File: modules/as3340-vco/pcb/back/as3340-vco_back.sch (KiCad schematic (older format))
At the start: 34 parts, among them J1 Conn_02x08_Odd_Even, J2 Conn_01x09, U1 AS3340, U2 L79L05_TO92

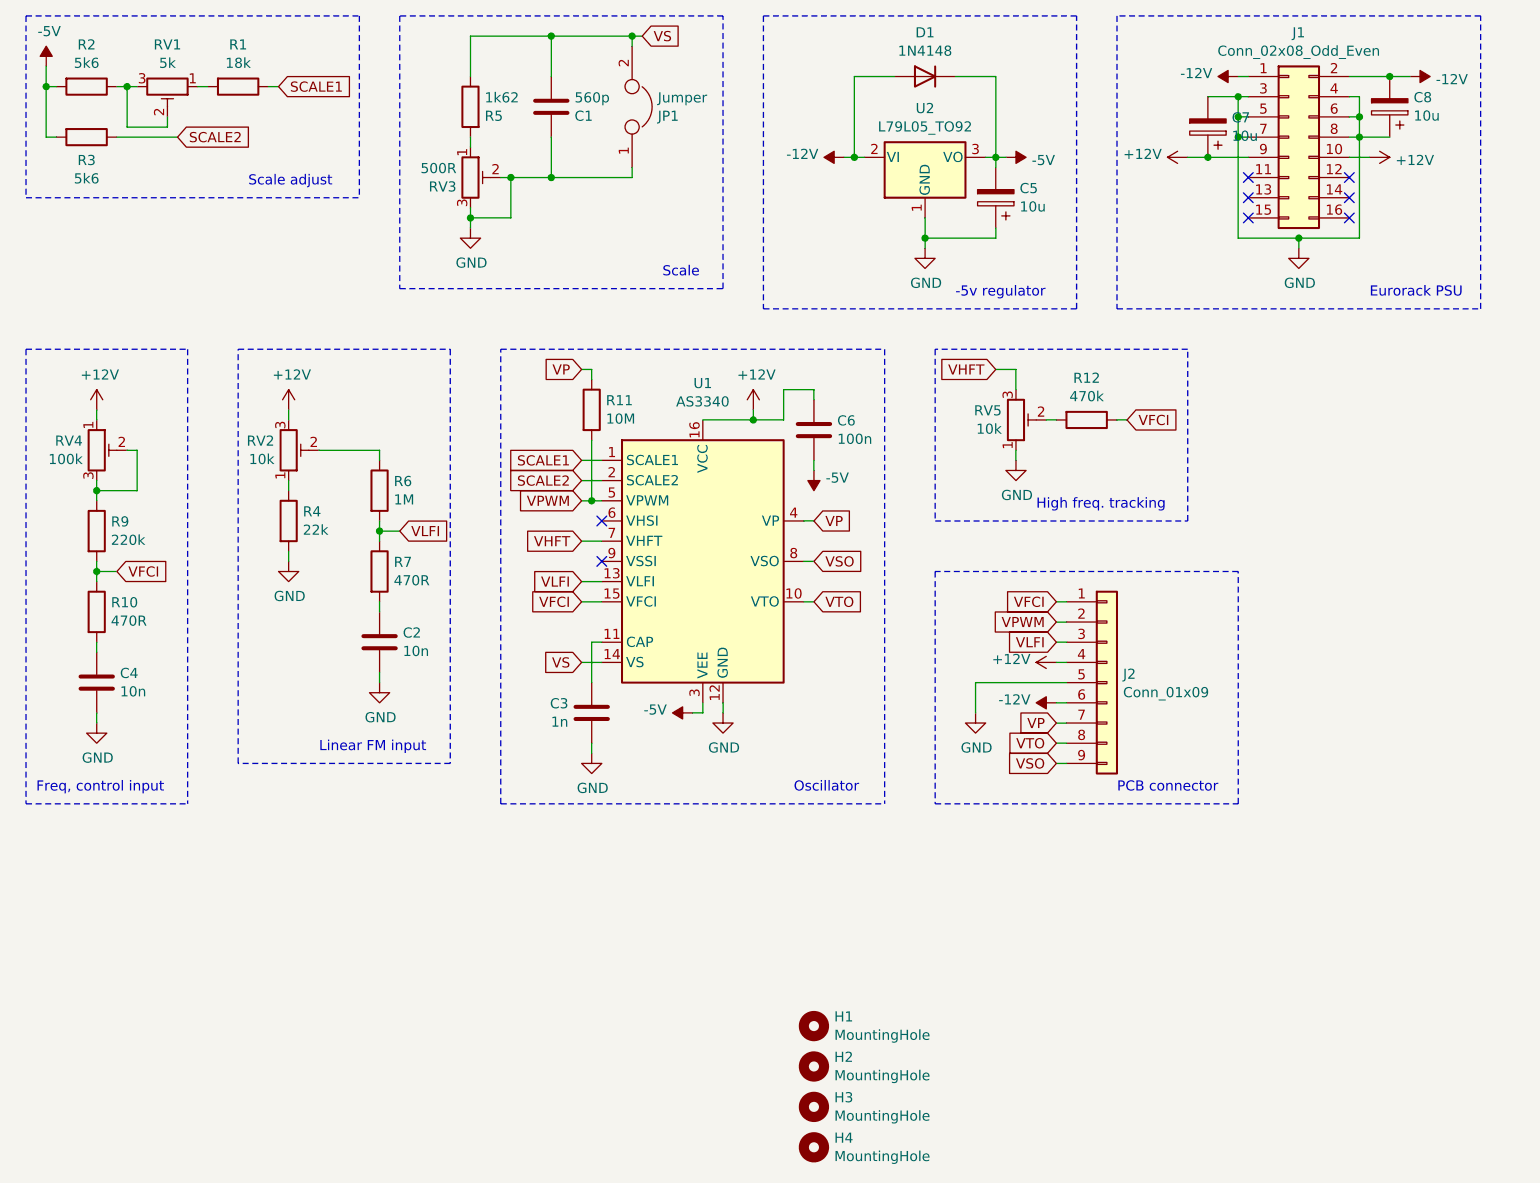
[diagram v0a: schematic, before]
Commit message: modules: as3340-vco: fix references
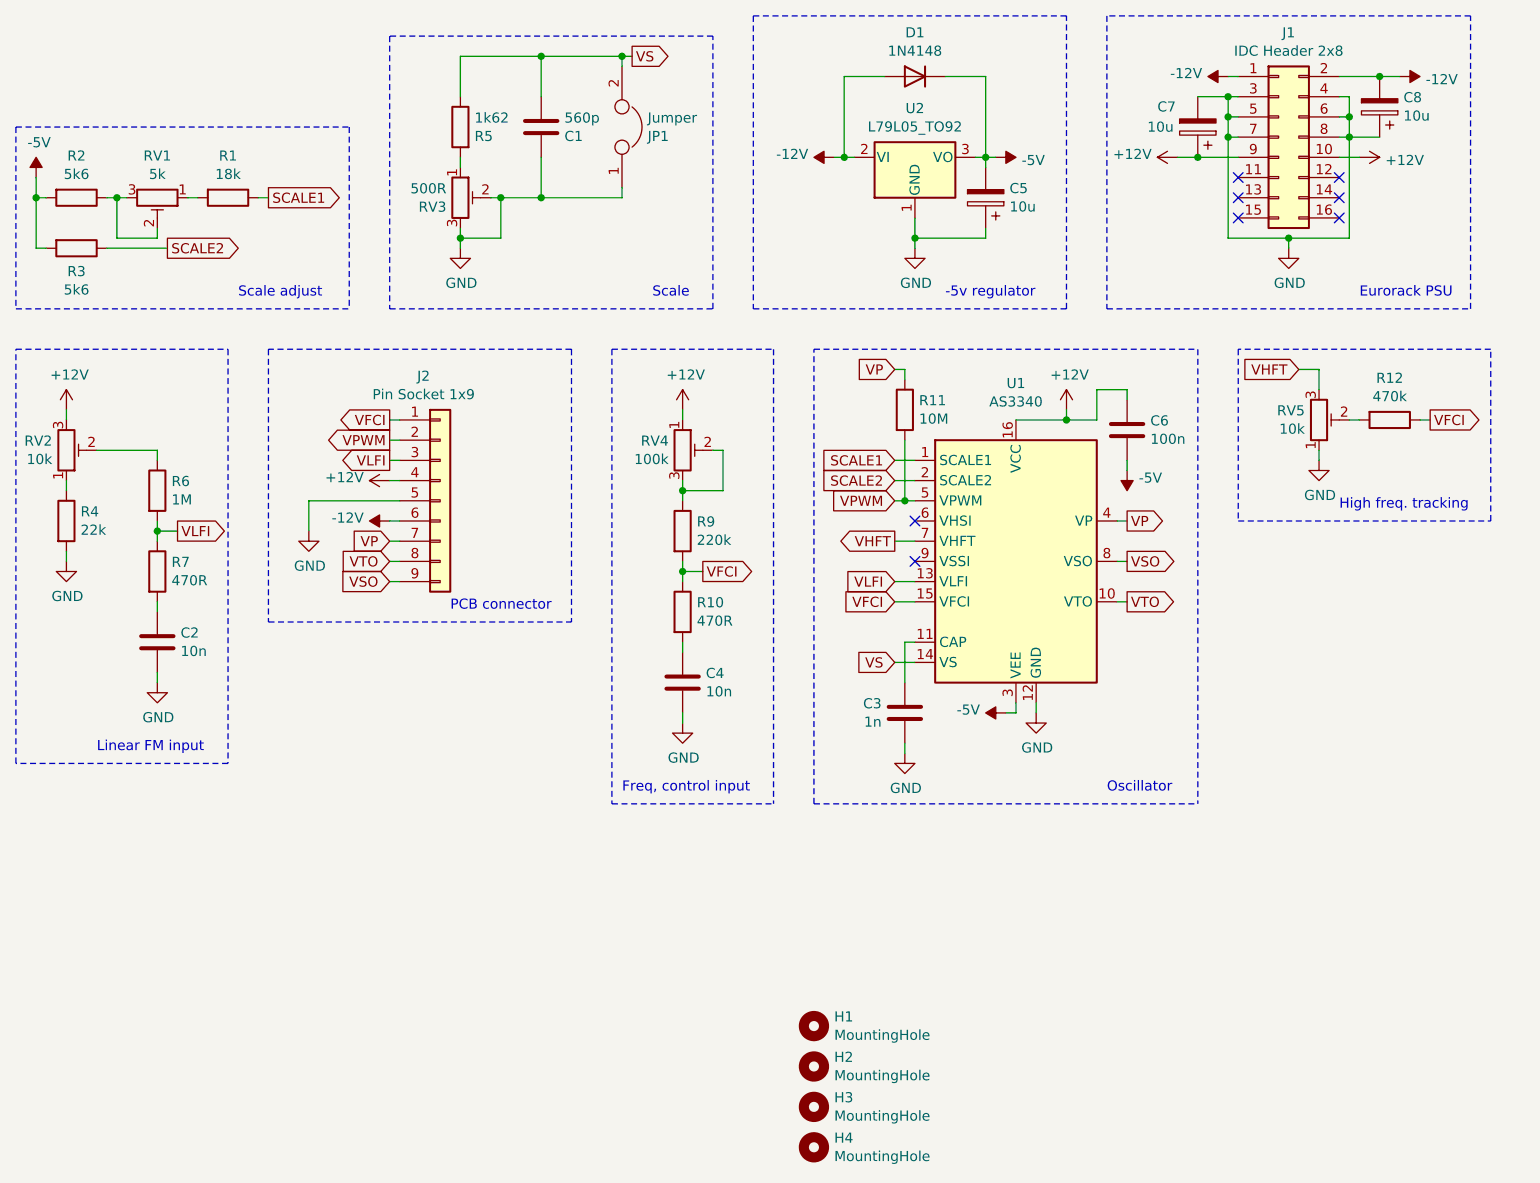
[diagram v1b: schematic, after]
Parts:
- J1: value Conn_02x08_Odd_Even -> IDC Header 2x8
- J2: value Conn_01x09 -> Pin Socket 1x9
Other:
- moved on the sheet: C1, C2, C3, C4, C5, C6, C7, C8, D1, J1, J2, JP1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
